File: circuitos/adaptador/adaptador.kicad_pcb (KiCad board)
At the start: 2 copper layers, 70 x 50 mm, 10 parts, among them J1 Screw_Terminal_01x02, J2 Screw_Terminal_01x02, U1 TL082

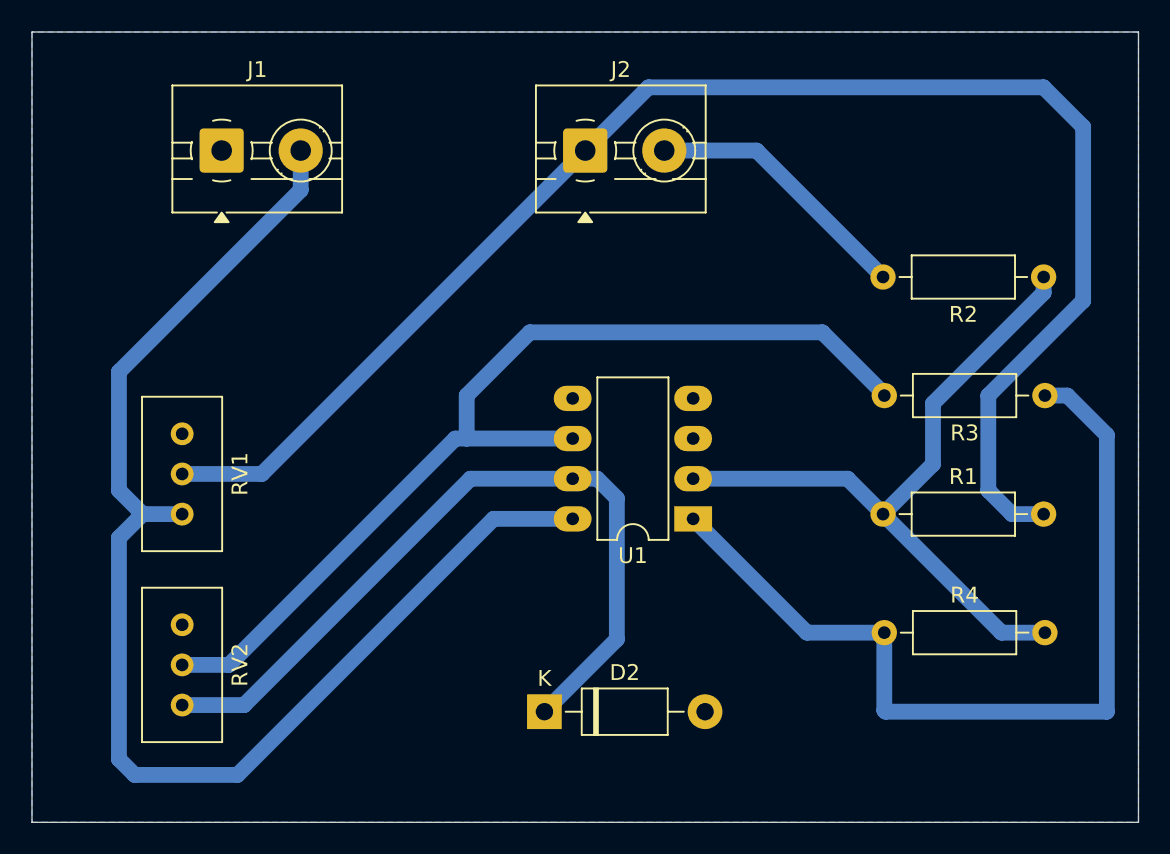
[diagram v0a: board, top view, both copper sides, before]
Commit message: update: resize dimensions for can print on CNC
- Resize on Edge Cuts layer
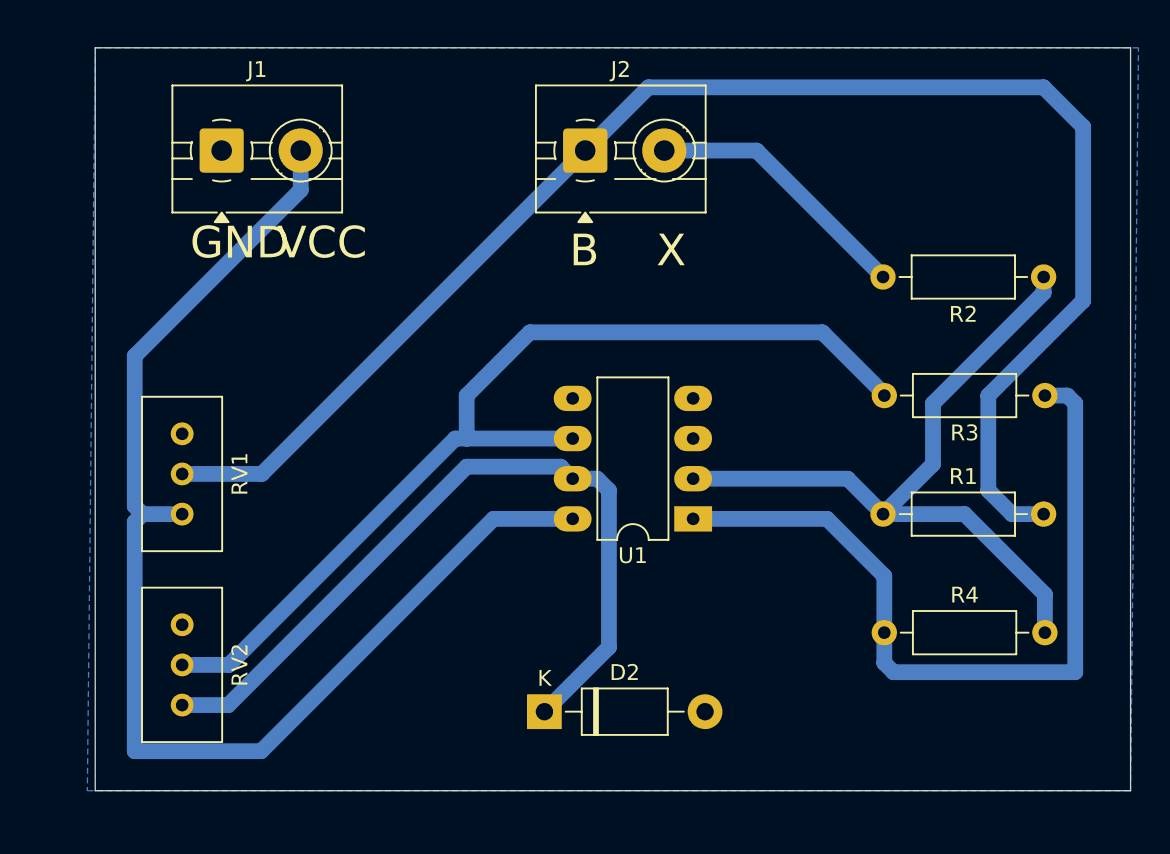
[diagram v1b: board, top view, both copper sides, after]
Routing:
- net Net-(R3-Pad1): track 56.6 -> 50.5 mm
- net VCC: track 82.8 -> 79.1 mm
- net Net-(U1A--): track 45.5 -> 46.9 mm
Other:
- board size 70 x 50 mm -> 65.5 x 47 mm
- board text added: "B"
- board text added: "GND"
- board text added: "VCC"
- board text added: "X"
